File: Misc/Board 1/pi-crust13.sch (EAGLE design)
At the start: 28 parts, among them U1 AD9983AKSTZ_140, U2 SN54LS253_J_16, U3 SN54LS253_J_16, U4 SN54LS253_J_16

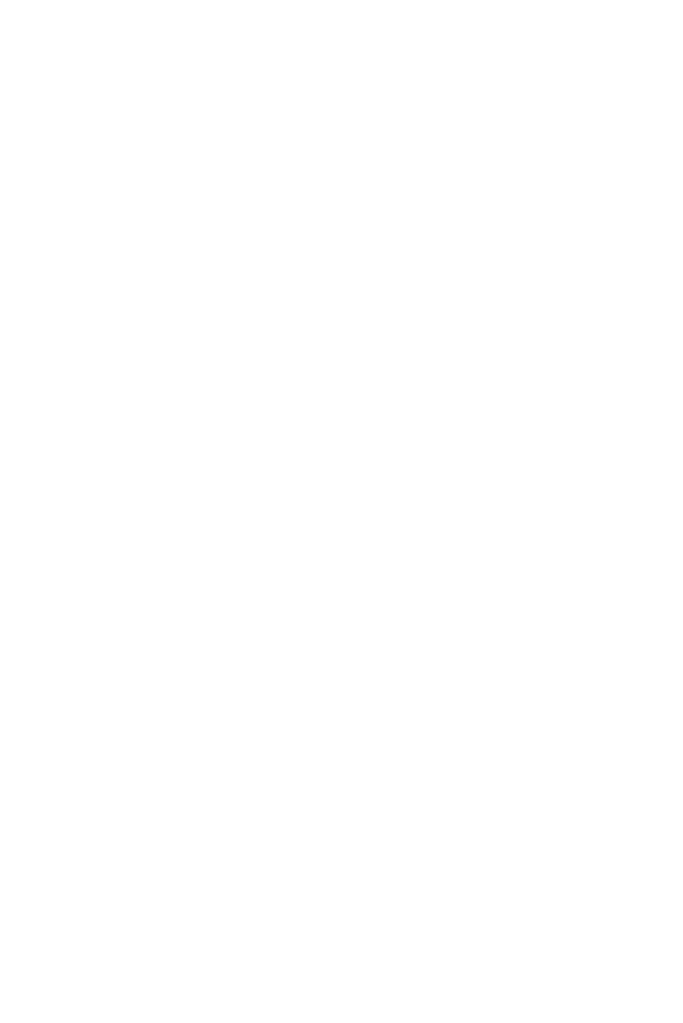
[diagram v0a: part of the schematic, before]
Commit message: Board Update
1.8V configured upon approval, D-Flip Flops added (choose optimal), Wire
configuration still not working correctly
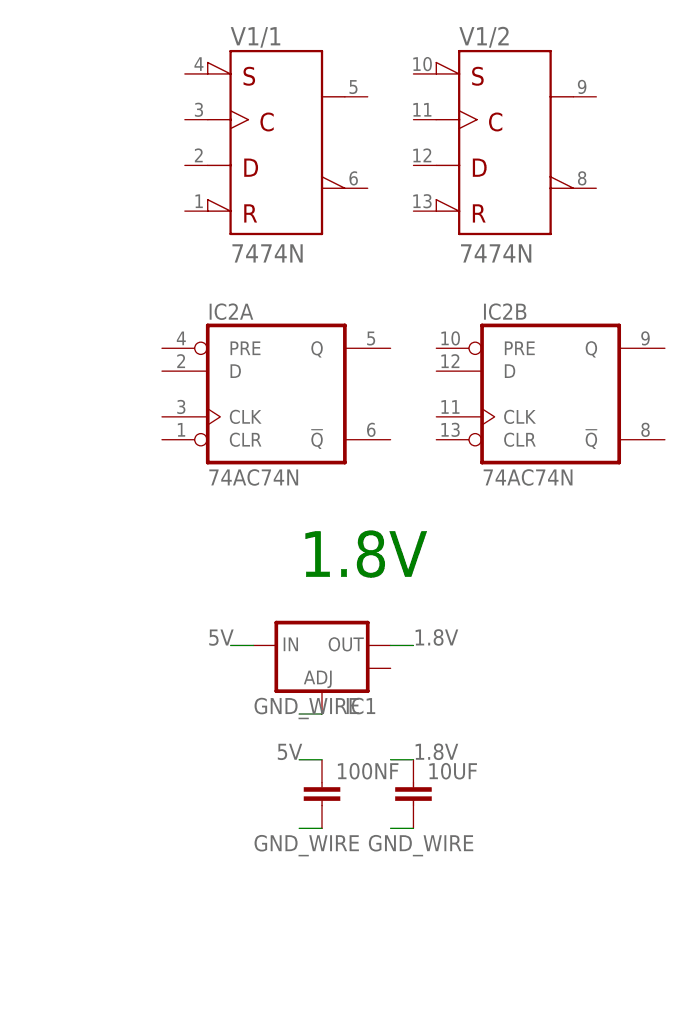
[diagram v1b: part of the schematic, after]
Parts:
- added 100NF, 10UF: (no value), capacitor-wima:C2.5/5
- added IC1: (no value), SparkFun-PowerIC:V_REG_LM1117SOT223
- added IC2: 74AC74N, 74xx-eu:74AC74N
- added V1: 7474N, 74ttl-din:7474N
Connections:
- net 1.8V: now also 10UF.1, IC1.OUT
- net 5V: now also 100NF.1, IC1.IN
- net GND_WIRE: now also 100NF.2, 10UF.2, IC1.ADJ
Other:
- note added: "1.8V"
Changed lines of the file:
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@@
 <part name="U3" library="MUX" deviceset="SN54LS253_J_16" device=""/>
 <part name="U4" library="MUX" deviceset="SN54LS253_J_16" device=""/>
+<part name="IC1" library="SparkFun-PowerIC" deviceset="V_REG_LM1117" device="SOT223"/>
+<part name="IC2" library="74xx-eu" deviceset="74*74" device="N" technology="AC"/>
+<part name="V1" library="74ttl-din" deviceset="74*74" device="N"/>
+<part name="100NF" library="capacitor-wima" deviceset="C" device="2.5/5"/>
+<part name="10UF" library="capacitor-wima" deviceset="C" device="2.5/5"/>
 </parts>
 <sheets>
@@
 <text x="144.78" y="177.8" size="5.08" layer="91">MUX</text>
 <text x="198.12" y="91.44" size="5.08" layer="91">Component Input</text>
+<text x="231.14" y="177.8" size="5.08" layer="91">1.8V</text>
 </plain>
 <instances>
@@
 <instance part="U3" gate="A" x="127" y="129.54"/>
 <instance part="U4" gate="A" x="127" y="93.98"/>
+<instance part="IC1" gate="G$1" x="233.68" y="170.18"/>
+<instance part="IC2" gate="A" x="228.6" y="198.12"/>
+<instance part="V1" gate="/1" x="228.6" y="226.06"/>
+<instance part="V1" gate="/2" x="254" y="226.06"/>
+<instance part="IC2" gate="B" x="259.08" y="198.12"/>
+<instance part="100NF" gate="G$1" x="233.68" y="154.94"/>
+<instance part="10UF" gate="G$1" x="243.84" y="154.94"/>
 </instances>
 <busses>
@@
 <pinref part="U4" gate="A" pin="VCC"/>
 </segment>
+<segment>
+<wire x1="233.68" y1="157.48" x2="231.14" y2="157.48" width="0.6096" layer="91"/>
+<label x="228.6" y="157.48" size="1.778" layer="95"/>
+<pinref part="100NF" gate="G$1" pin="1"/>
+</segment>
+<segment>
+<wire x1="226.06" y1="170.18" x2="223.52" y2="170.18" width="0.6096" layer="91"/>
+<label x="220.98" y="170.18" size="1.778" layer="95"/>
+<pinref part="IC1" gate="G$1" pin="IN"/>
+</segment>
 </net>
 <net name="GND_WIRE" class="0">
@@
 <label x="104.14" y="15.24" size="1.778" layer="95"/>
 </segment>
+<segment>
+<wire x1="233.68" y1="149.86" x2="231.14" y2="149.86" width="0.8128" layer="91"/>
+<label x="226.06" y="147.32" size="1.778" layer="95"/>
+<pinref part="100NF" gate="G$1" pin="2"/>
+</segment>
+<segment>
+<wire x1="243.84" y1="149.86" x2="241.3" y2="149.86" width="0.8128" layer="91"/>
+<label x="238.76" y="147.32" size="1.778" layer="95"/>
+<pinref part="10UF" gate="G$1" pin="2"/>
+</segment>
+<segment>
+<wire x1="233.68" y1="162.56" x2="231.14" y2="162.56" width="0.8128" layer="91"/>
+<label x="226.06" y="162.56" size="1.778" layer="95"/>
+<pinref part="IC1" gate="G$1" pin="ADJ"/>
+</segment>
 </net>
 <net name="S0" class="0">
@@
 <wire x1="7.62" y1="132.08" x2="10.16" y2="132.08" width="0.6096" layer="91"/>
 </segment>
-</net>
+<segment>
+<wire x1="241.3" y1="170.18" x2="243.84" y2="170.18" width="0.6096" layer="91"/>
+<label x="243.84" y="170.18" size="1.778" layer="95"/>
+<pinref part="IC1" gate="G$1" pin="OUT"/>
+</segment>
+<segment>
+<wire x1="241.3" y1="157.48" x2="243.84" y2="157.48" width="0.6096" layer="91"/>
+<label x="243.84" y="157.48" size="1.778" layer="95"/>
+<pinref part="10UF" gate="G$1" pin="1"/>
+</segment>
+</net>
